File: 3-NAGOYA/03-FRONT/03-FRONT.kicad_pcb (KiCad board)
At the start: 2 copper layers, 110 x 30 mm, 31 parts, among them J1 OpenMV Conn, J2 PC-PD, J3 WRITER CONN, J4 PA0-7, J5 PB3-9, U6 STM32F103C8Tx, U7 AMS1117-3.3

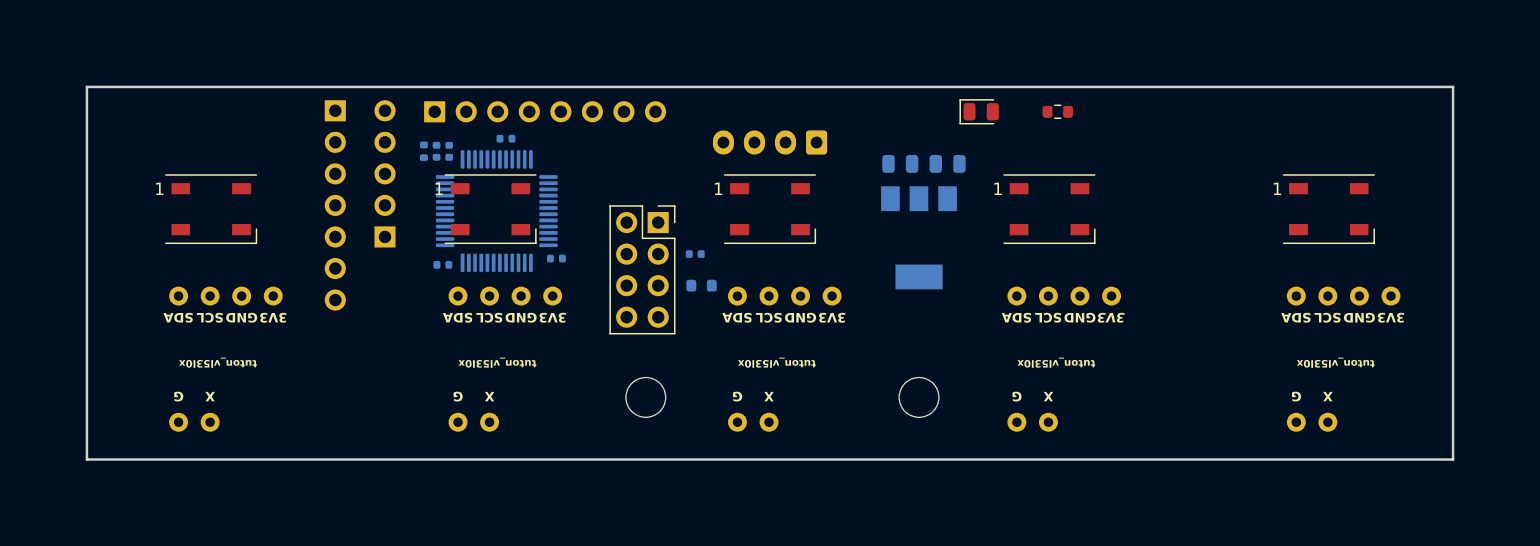
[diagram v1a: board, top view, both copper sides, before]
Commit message: 03-FRONT XIAOに変更
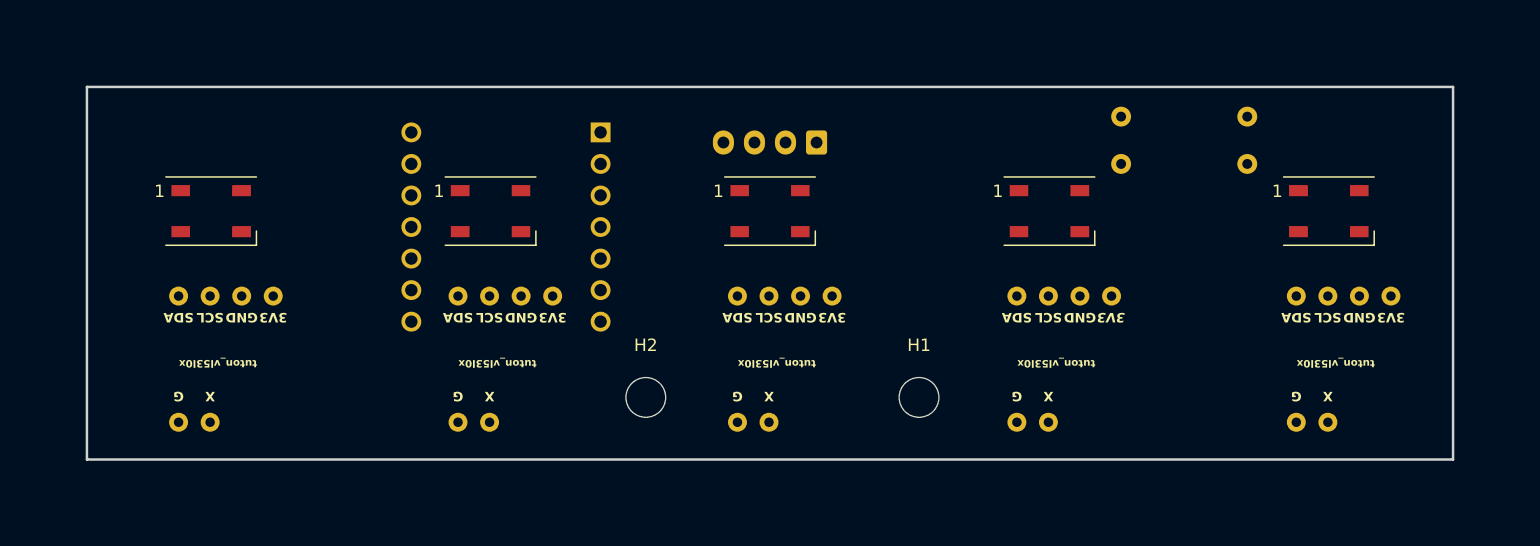
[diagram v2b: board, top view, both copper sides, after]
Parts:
- removed C1, C2, C3, C4, C5, C6: 100n, Capacitor_SMD:C_0402_1005Metric
- removed C7: 4.7u, Resistor_SMD:R_0402_1005Metric
- removed C8, C9: 22u, Capacitor_SMD:C_0805_2012Metric
- removed D6: WS2812B, LED_SMD:LED_WS2812B_PLCC4_5.0x5.0mm_P3.2mm
- removed J2: PC-PD, Connector_PinHeader_2.54mm:PinHeader_1x05_P2.54mm_Vertical
- removed J3: WRITER CONN, Connector_PinSocket_2.54mm:PinSocket_2x04_P2.54mm_Vertical
- removed J4: PA0-7, Connector_PinHeader_2.54mm:PinHeader_1x08_P2.54mm_Vertical
- removed J5: PB3-9, Connector_PinHeader_2.54mm:PinHeader_1x07_P2.54mm_Vertical
- removed R3: 470, Resistor_SMD:R_0603_1608Metric
- removed REF** (x2): MountingHole_3.2mm_M3, MountingHole:MountingHole_3.2mm_M3
- removed U7: AMS1117-3.3, Package_TO_SOT_SMD:SOT-223-3_TabPin2
- added H1: MountingHole, MountingHole:MountingHole_3.2mm_M3, F.Cu at (112.0, 95.0)
- added H2: MountingHole, MountingHole:MountingHole_3.2mm_M3, F.Cu at (90.0, 95.0)
- added R1: 10k, Resistor_THT:R_Axial_DIN0207_L6.3mm_D2.5mm_P10.16mm_Horizontal, B.Cu at (138.4, 72.4)
- D1: value LED_GREEN -> WS2812B; footprint LED_SMD:LED_0805_2012Metric -> LED_SMD:LED_WS2812B_PLCC4_5.0x5.0mm_P3.2mm
- R2: footprint Resistor_SMD:R_0603_1608Metric -> Resistor_THT:R_Axial_DIN0207_L6.3mm_D2.5mm_P10.16mm_Horizontal
- U6: value STM32F103C8Tx -> ~; footprint Package_QFP:LQFP-48_7x7mm_P0.5mm -> XIAO:MOUDLE14P-2.54-21X17.8MM
- moved D1 62.5 mm to (55.0, 80.0)
- moved R2 35.2 mm to (128.3, 76.2)
- moved D2 22.5 mm to (77.5, 80.0)
- moved D3 22.5 mm to (100.0, 80.0)
- moved D4 22.5 mm to (122.5, 80.0)
- moved D5 22.5 mm to (145.0, 80.0)
- moved U6 1.48 mm to (78.7, 81.3), turned to 90 degrees
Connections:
- D1 pad 1: Net-(D1-K) -> +5V
- D1 pad 2: +3V3 -> Net-(D1-DOUT)
- D2 pad 4: WS2812B -> Net-(D1-DOUT)
- D5 pad 2: Net-(D5-DOUT) -> unconnected-(D5-DOUT-Pad2)
- J1 pad 2: UART3_RX -> RX
- J1 pad 3: UART3_TX -> TX
- R2 pad 1: BOOT0 -> SDA
- R2 pad 2: GND -> +3V3
- U6 pad 1: +3V3 -> XSHUT1
- U6 pad 10: Net-(J4-Pin_1) -> WS2812B
- U6 pad 11: Net-(J4-Pin_2) -> unconnected-(U6-D10-Pad11)
- U6 pad 12: Net-(J4-Pin_3) -> unconnected-(U6-3V3-Pad12)
- U6 pad 13: Net-(J4-Pin_4) -> unconnected-(U6-GND-Pad13)
- U6 pad 14: Net-(J4-Pin_5) -> unconnected-(U6-5V-Pad14)
- U6 pad 2: Net-(J2-Pin_3) -> XSHUT1
- U6 pad 3: Net-(J2-Pin_2) -> XSHUT1
- U6 pad 4: Net-(J2-Pin_1) -> XSHUT1
- U6 pad 5: Net-(J2-Pin_5) -> SDA
- U6 pad 6: Net-(J2-Pin_4) -> SCL
- U6 pad 7: NRST -> TX
- U6 pad 8: GND -> RX
- U6 pad 9: +3V3 -> XSHUT1

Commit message: 06-UI完成
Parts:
- added G***: LOGO, logo:tuton_logo, B.Cu at (145.0, 78.2)
- added G***: LOGO, logo:st_logo, B.Cu at (135.9, 81.3)
- added G***: LOGO, logo:jlcpcb_logo, B.Cu at (130.6, 76.7)
- moved R1 26.0 mm to (114.6, 82.8), turned to 90 degrees
- moved R2 18.3 mm to (111.3, 82.8), turned to 90 degrees
- moved D1 2.00 mm to (57.0, 80.0)
- moved U1 0.81 mm to (60.8, 86.8)
- moved U6 0.76 mm to (78.7, 80.5)
- moved U5 0.38 mm to (149.6, 86.8)
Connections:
- U6 pad 12: unconnected-(U6-3V3-Pad12) -> +3V3
- U6 pad 13: unconnected-(U6-GND-Pad13) -> GND
- U6 pad 14: unconnected-(U6-5V-Pad14) -> +5V
- U6 pad 2: XSHUT1 -> XSHUT2
- U6 pad 3: XSHUT1 -> XSHUT3
- U6 pad 4: XSHUT1 -> XSHUT4
- U6 pad 9: XSHUT1 -> XSHUT5
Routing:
- net +3V3: track 0.00 -> 172.4 mm
- net +5V: track 0.00 -> 106.6 mm
- net SCL: track 0.00 -> 106.0 mm
- net SDA: track 0.00 -> 102.2 mm
- net XSHUT5: track 0.00 -> 86.1 mm
- net XSHUT4: track 0.00 -> 45.0 mm
- net XSHUT1: track 0.00 -> 40.8 mm
- net RX: track 0.00 -> 37.6 mm
- net XSHUT3: track 0.00 -> 35.9 mm
- net Net-(D2-DOUT): track 0.00 -> 30.5 mm
- net Net-(D1-DOUT): track 0.00 -> 29.4 mm
- net Net-(D3-DOUT): track 0.00 -> 28.8 mm
- net Net-(D4-DOUT): track 0.00 -> 28.8 mm
- net TX: track 0.00 -> 27.2 mm
- net XSHUT2: track 0.00 -> 25.3 mm
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- added copper zone on B.Cu, net GND
- added copper zone on F.Cu, net GND
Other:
- board size 110 x 30 mm -> 100 x 30 mm
- board text added: "3V3"
- board text added: "5V"
- board text added: "GND"
- board text added: "I2C 10k"
- board text added: "LED"
- board text added: "RX"
- board text added: "SCL"
- board text added: "SDA"
- board text added: "TX"
- board text added: "Tuton 2025 03-FRONT"
- board text added: "X1"
- board text added: "X2"
- board text added: "X3"
- board text added: "X4"
- board text added: "X5"
- board text added: "①"
- board text added: "②"
- board text added: "③"
- board text added: "④"
- board text added: "⑤"
